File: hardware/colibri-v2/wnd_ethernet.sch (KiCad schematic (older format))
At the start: 4 parts

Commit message: Annotated Components
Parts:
- gave numbers to parts that had none: 4
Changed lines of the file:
@@
 $EndDescr
 $Comp
-L 7499111121A LAN?
+L 7499111121A LAN1
 U 1 1 56176AEE
 P 6350 3800
-F 0 "LAN?" H 6750 4900 60  0000 C CNN
+F 0 "LAN1" H 6750 4900 60  0000 C CNN
 F 1 "7499111121A" H 6150 4900 60  0000 C CNN
 F 2 "" H 6350 4250 60  0000 C CNN
@@
 	3150 3850 5650 3850
 $Comp
-L C C?
+L C C67
 U 1 1 5617727F
 P 4250 4050
-F 0 "C?" V 4200 4100 50  0000 L CNN
+F 0 "C67" V 4200 4100 50  0000 L CNN
 F 1 "100n/50V" V 4200 3600 50  0000 L CNN
 F 2 "" H 4288 3900 30  0000 C CNN
@@
 	3800 4150 5650 4150
 $Comp
-L GND #PWR?
+L GND #PWR103
 U 1 1 561772BC
 P 5000 5150
-F 0 "#PWR?" H 5000 4900 50  0001 C CNN
+F 0 "#PWR103" H 5000 4900 50  0001 C CNN
 F 1 "GND" H 5000 5000 50  0000 C CNN
 F 2 "" H 5000 5150 60  0000 C CNN
@@
 Connection ~ 5000 4150
 $Comp
-L +3V3 #PWR?
+L +3V3 #PWR104
 U 1 1 561773DA
 P 5250 2300
-F 0 "#PWR?" H 5250 2150 50  0001 C CNN
+F 0 "#PWR104" H 5250 2150 50  0001 C CNN
 F 1 "+3V3" H 5250 2440 50  0000 C CNN
 F 2 "" H 5250 2300 60  0000 C CNN
@@
 Connection ~ 5250 4350
 $Comp
-L R R?
+L R R76
 U 1 1 56177409
 P 4250 4750
-F 0 "R?" V 4330 4750 50  0000 C CNN
+F 0 "R76" V 4330 4750 50  0000 C CNN
 F 1 "100" V 4250 4750 50  0000 C CNN
 F 2 "" V 4180 4750 30  0000 C CNN
@@
 $EndComp
 $Comp
-L R R?
+L R R77
 U 1 1 56177461
 P 4250 4900
-F 0 "R?" V 4330 4900 50  0000 C CNN
+F 0 "R77" V 4330 4900 50  0000 C CNN
 F 1 "100" V 4250 4900 50  0000 C CNN
 F 2 "" V 4180 4900 30  0000 C CNN

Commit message: Work on hardware
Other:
- note added: "To optimize the size"
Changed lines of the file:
@@
 	4700 4900 4700 4750
 Connection ~ 4700 4750
+Text Notes 7000 3850 0    120  ~ 24
+To optimize the size
 $EndSCHEMATC

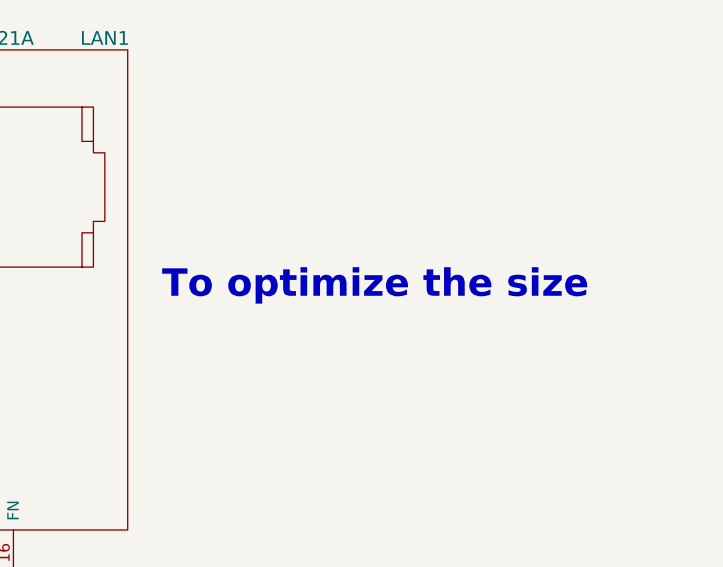
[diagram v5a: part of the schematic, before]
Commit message: Reworked the buttons/leds sheet
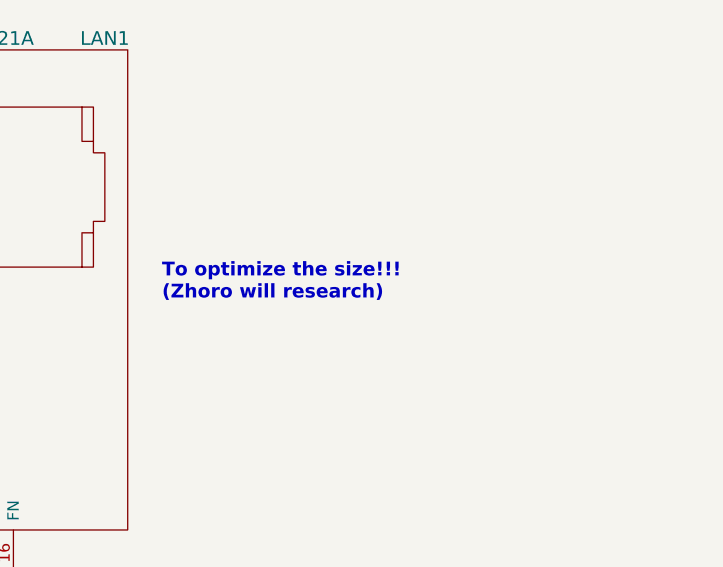
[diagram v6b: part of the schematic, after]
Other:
- note added: "To optimize the size!!!\n(Zhoro will research)"
- note removed: "To optimize the size"
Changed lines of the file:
@@
 	4700 4900 4700 4750
 Connection ~ 4700 4750
-Text Notes 7000 3850 0    120  ~ 24
-To optimize the size
+Text Notes 7000 3850 0    60   ~ 12
+To optimize the size!!!\n(Zhoro will research)
 $EndSCHEMATC

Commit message: Re-annotated schematic
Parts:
- renumbered C67 to C65, R76 to R77, R77 to R78
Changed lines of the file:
@@
 	3150 3850 5650 3850
 $Comp
-L C C67
+L C C65
 U 1 1 5617727F
 P 4250 4050
-F 0 "C67" V 4200 4100 50  0000 L CNN
+F 0 "C65" V 4200 4100 50  0000 L CNN
 F 1 "100n/50V" V 4200 3600 50  0000 L CNN
 F 2 "" H 4288 3900 30  0000 C CNN
@@
 	3800 4150 5650 4150
 $Comp
-L GND #PWR0105
+L GND #PWR100
 U 1 1 561772BC
 P 5000 5150
-F 0 "#PWR0105" H 5000 4900 50  0001 C CNN
+F 0 "#PWR100" H 5000 4900 50  0001 C CNN
 F 1 "GND" H 5000 5000 50  0000 C CNN
 F 2 "" H 5000 5150 60  0000 C CNN
@@
 Connection ~ 5000 4150
 $Comp
-L +3V3 #PWR0106
+L +3V3 #PWR101
 U 1 1 561773DA
 P 5250 2300
-F 0 "#PWR0106" H 5250 2150 50  0001 C CNN
+F 0 "#PWR101" H 5250 2150 50  0001 C CNN
 F 1 "+3V3" H 5250 2440 50  0000 C CNN
 F 2 "" H 5250 2300 60  0000 C CNN
@@
 Connection ~ 5250 4350
 $Comp
-L R R76
+L R R77
 U 1 1 56177409
 P 4250 4750
-F 0 "R76" V 4330 4750 50  0000 C CNN
+F 0 "R77" V 4330 4750 50  0000 C CNN
 F 1 "100" V 4250 4750 50  0000 C CNN
 F 2 "" V 4180 4750 30  0000 C CNN
@@
 $EndComp
 $Comp
-L R R77
+L R R78
 U 1 1 56177461
 P 4250 4900
-F 0 "R77" V 4330 4900 50  0000 C CNN
+F 0 "R78" V 4330 4900 50  0000 C CNN
 F 1 "100" V 4250 4900 50  0000 C CNN
 F 2 "" V 4180 4900 30  0000 C CNN

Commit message: Associated footprints for R and some of the C
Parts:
- R77, R78: footprint (none) -> Resistors_SMD:R_0603
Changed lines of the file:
@@
 F 0 "LAN1" H 6750 4900 60  0000 C CNN
 F 1 "7499111121A" H 6150 4900 60  0000 C CNN
-F 2 "" H 6350 4250 60  0000 C CNN
+F 2 "" H 6350 4250 60  0001 C CNN
 F 3 "" H 6350 4250 60  0000 C CNN
 	1    6350 3800
@@
 F 0 "C65" V 4200 4100 50  0000 L CNN
 F 1 "100n/50V" V 4200 3600 50  0000 L CNN
-F 2 "" H 4288 3900 30  0000 C CNN
+F 2 "" H 4288 3900 30  0001 C CNN
 F 3 "" H 4250 4050 60  0000 C CNN
 	1    4250 4050
@@
 	3800 4150 5650 4150
 $Comp
-L GND #PWR100
+L GND #PWR0102
 U 1 1 561772BC
 P 5000 5150
-F 0 "#PWR100" H 5000 4900 50  0001 C CNN
+F 0 "#PWR0102" H 5000 4900 50  0001 C CNN
 F 1 "GND" H 5000 5000 50  0000 C CNN
 F 2 "" H 5000 5150 60  0000 C CNN
@@
 Connection ~ 5000 4150
 $Comp
-L +3V3 #PWR101
+L +3V3 #PWR0103
 U 1 1 561773DA
 P 5250 2300
-F 0 "#PWR101" H 5250 2150 50  0001 C CNN
+F 0 "#PWR0103" H 5250 2150 50  0001 C CNN
 F 1 "+3V3" H 5250 2440 50  0000 C CNN
 F 2 "" H 5250 2300 60  0000 C CNN
@@
 F 0 "R77" V 4330 4750 50  0000 C CNN
 F 1 "100" V 4250 4750 50  0000 C CNN
-F 2 "" V 4180 4750 30  0000 C CNN
+F 2 "Resistors_SMD:R_0603" V 4180 4750 30  0001 C CNN
 F 3 "" H 4250 4750 30  0000 C CNN
 	1    4250 4750
@@
 F 0 "R78" V 4330 4900 50  0000 C CNN
 F 1 "100" V 4250 4900 50  0000 C CNN
-F 2 "" V 4180 4900 30  0000 C CNN
+F 2 "Resistors_SMD:R_0603" V 4180 4900 30  0001 C CNN
 F 3 "" H 4250 4900 30  0000 C CNN
 	1    4250 4900
